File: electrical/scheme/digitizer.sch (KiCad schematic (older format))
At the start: 175 parts, among them P1 mode, P10 in-2, P11 in-3, P12 in-1, P13 USB_B, P14 screw, P15 screw, P16 screw, P17 screw, P2 ~rst~, P3 ext, P4 trig, P5 trig-mode, P6 swd, P7 out-0, P8 out-1, P9 in-0, U1 AD8672, U10 crystal-4pin, U100 AD8672, U101 AD8672, U11 CP2102, U12 adr4533, U13 BAT54S, U14 adr4533, U15 ADT7410, U16 MCP1703T-3302E/CB, U17 AD7683, U18 NCP3063, U19 ADG5204, U2 AD8672, U20 NCP3063, U3 AD8672

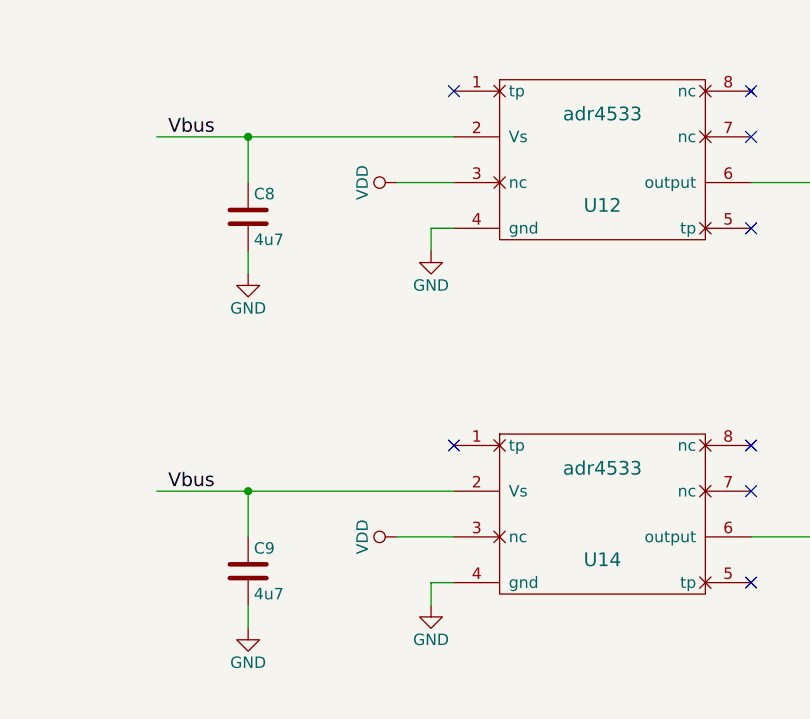
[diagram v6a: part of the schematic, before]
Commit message: Placed all components. Now routing.
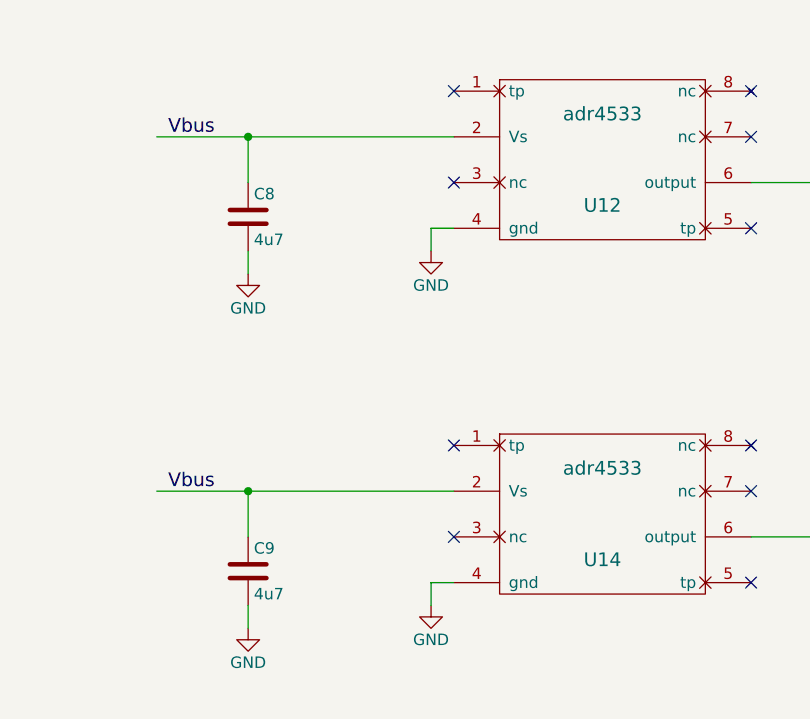
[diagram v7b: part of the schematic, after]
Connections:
- wire segments 573 -> 571
- no-connect marks 18 -> 20
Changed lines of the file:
@@
-$EndComp
-Wire Wire Line
-	7850 15150 7600 15150
-$Comp
-L VDD #PWR0120
-U 1 1 55A8AFAB
-P 7600 15150
-F 0 "#PWR0120" H 7600 15000 50  0001 C CNN
-F 1 "VDD" H 7600 15300 50  0000 C CNN
-F 2 "" H 7600 15150 60  0000 C CNN
-F 3 "" H 7600 15150 60  0000 C CNN
-	1    7600 15150
-	0    -1   -1   0
 $EndComp
 Wire Wire Line
@@
 	7750 15350 7750 15450
 $Comp
-L GND #PWR0121
+L GND #PWR0120
 U 1 1 55A8B562
 P 7750 15450
-F 0 "#PWR0121" H 7750 15200 50  0001 C CNN
+F 0 "#PWR0120" H 7750 15200 50  0001 C CNN
 F 1 "GND" H 7750 15300 50  0000 C CNN
 F 2 "" H 7750 15450 60  0000 C CNN
@@
 $EndComp
 $Comp
-L GND #PWR0122
+L GND #PWR0121
 U 1 1 55A8EB1B
 P 6950 17100
-F 0 "#PWR0122" H 6950 16850 50  0001 C CNN
+F 0 "#PWR0121" H 6950 16850 50  0001 C CNN
 F 1 "GND" H 6950 16950 50  0000 C CNN
 F 2 "" H 6950 17100 60  0000 C CNN
@@
 Connection ~ 6950 16500
 Wire Wire Line
-	7850 16700 7600 16700
-$Comp
-L VDD #PWR0123
-U 1 1 55A8EB27
-P 7600 16700
-F 0 "#PWR0123" H 7600 16550 50  0001 C CNN
-F 1 "VDD" H 7600 16850 50  0000 C CNN
-F 2 "" H 7600 16700 60  0000 C CNN
-F 3 "" H 7600 16700 60  0000 C CNN
-	1    7600 16700
-	0    -1   -1   0
-$EndComp
-Wire Wire Line
 	7850 16900 7750 16900
 Wire Wire Line
 	7750 16900 7750 17000
 $Comp
-L GND #PWR0124
+L GND #PWR0122
 U 1 1 55A8EB2F
 P 7750 17000
-F 0 "#PWR0124" H 7750 16750 50  0001 C CNN
+F 0 "#PWR0122" H 7750 16750 50  0001 C CNN
 F 1 "GND" H 7750 16850 50  0000 C CNN
 F 2 "" H 7750 17000 60  0000 C CNN
@@
 Connection ~ 11850 16150
 $Comp
-L GND #PWR0125
+L GND #PWR0123
 U 1 1 55AF854A
 P 11850 16300
-F 0 "#PWR0125" H 11850 16050 50  0001 C CNN
+F 0 "#PWR0123" H 11850 16050 50  0001 C CNN
 F 1 "GND" H 11850 16150 50  0000 C CNN
 F 2 "" H 11850 16300 60  0000 C CNN
@@
 	13450 16600 13450 16700
 $Comp
-L GND #PWR0126
+L GND #PWR0124
 U 1 1 55B009F0
 P 13300 16700
-F 0 "#PWR0126" H 13300 16450 50  0001 C CNN
+F 0 "#PWR0124" H 13300 16450 50  0001 C CNN
 F 1 "GND" H 13300 16550 50  0000 C CNN
 F 2 "" H 13300 16700 60  0000 C CNN
@@
 $EndComp
 $Comp
-L GND #PWR0127
+L GND #PWR0125
 U 1 1 55B00B93
 P 13450 16700
-F 0 "#PWR0127" H 13450 16450 50  0001 C CNN
+F 0 "#PWR0125" H 13450 16450 50  0001 C CNN
 F 1 "GND" H 13450 16550 50  0000 C CNN
 F 2 "" H 13450 16700 60  0000 C CNN
@@
 	13600 15750 13600 15900
 $Comp
-L GND #PWR0128
+L GND #PWR0126
 U 1 1 55B012C1
 P 13600 15900
-F 0 "#PWR0128" H 13600 15650 50  0001 C CNN
+F 0 "#PWR0126" H 13600 15650 50  0001 C CNN
 F 1 "GND" H 13600 15750 50  0000 C CNN
 F 2 "" H 13600 15900 60  0000 C CNN
@@
 	13300 15550 13300 15400
 $Comp
-L VDD #PWR0129
+L VDD #PWR0127
 U 1 1 55B03BC9
 P 13300 15400
-F 0 "#PWR0129" H 13300 15250 50  0001 C CNN
+F 0 "#PWR0127" H 13300 15250 50  0001 C CNN
 F 1 "VDD" H 13300 15550 50  0000 C CNN
 F 2 "" H 13300 15400 60  0000 C CNN
@@
 	13900 16000 13900 16150
 $Comp
-L GND #PWR0130
+L GND #PWR0128
 U 1 1 55B0B079
 P 13900 16150
-F 0 "#PWR0130" H 13900 15900 50  0001 C CNN
+F 0 "#PWR0128" H 13900 15900 50  0001 C CNN
 F 1 "GND" H 13900 16000 50  0000 C CNN
 F 2 "" H 13900 16150 60  0000 C CNN
@@
 	30450 15350 30450 15550
 $Comp
-L GND #PWR0131
+L GND #PWR0129
 U 1 1 55C1E9F0
 P 30450 15550
-F 0 "#PWR0131" H 30450 15300 50  0001 C CNN
+F 0 "#PWR0129" H 30450 15300 50  0001 C CNN
 F 1 "GND" H 30450 15400 50  0000 C CNN
 F 2 "" H 30450 15550 60  0000 C CNN
@@
 	30650 15350 30650 15550
 $Comp
-L GND #PWR0132
+L GND #PWR0130
 U 1 1 55C1EC48
 P 30650 15550
-F 0 "#PWR0132" H 30650 15300 50  0001 C CNN
+F 0 "#PWR0130" H 30650 15300 50  0001 C CNN
 F 1 "GND" H 30650 15400 50  0000 C CNN
 F 2 "" H 30650 15550 60  0000 C CNN
@@
 	30850 15350 30850 15550
 $Comp
-L GND #PWR0133
+L GND #PWR0131
 U 1 1 55C1EEA3
 P 30850 15550
-F 0 "#PWR0133" H 30850 15300 50  0001 C CNN
+F 0 "#PWR0131" H 30850 15300 50  0001 C CNN
 F 1 "GND" H 30850 15400 50  0000 C CNN
 F 2 "" H 30850 15550 60  0000 C CNN
@@
 	31050 15350 31050 15550
 $Comp
-L GND #PWR0134
+L GND #PWR0132
 U 1 1 55C1EEB0
 P 31050 15550
-F 0 "#PWR0134" H 31050 15300 50  0001 C CNN
+F 0 "#PWR0132" H 31050 15300 50  0001 C CNN
 F 1 "GND" H 31050 15400 50  0000 C CNN
 F 2 "" H 31050 15550 60  0000 C CNN
@@
 Wire Wire Line
 	23600 2650 24400 2650
+NoConn ~ 7850 16700
+NoConn ~ 7850 15150
 $EndSCHEMATC

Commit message: a
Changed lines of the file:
@@
 Text Label 4150 5900 0    60   ~ 0
 led-0
-Text Label 4150 6600 0    60   ~ 0
+Text Label 9800 2300 0    60   ~ 0
 led-1
 $Comp
@@
 Text Label 9800 3200 0    60   ~ 0
 rx-2
-Text Label 9800 2300 0    60   ~ 0
+Text Label 4150 6600 0    60   ~ 0
 gpio-0
-Text Label 9800 6950 0    60   ~ 0
+Text Label 9700 8100 0    60   ~ 0
 gpio-1
-Text Label 9800 7150 0    60   ~ 0
+Text Label 9700 7500 0    60   ~ 0
 gpio-2
-Text Label 9800 7500 0    60   ~ 0
+Text Label 9700 6950 0    60   ~ 0
 gpio-3
-Text Label 9800 8100 0    60   ~ 0
+Text Label 9700 7150 0    60   ~ 0
 gpio-4
 Text Label 2700 12550 0    60   ~ 0
